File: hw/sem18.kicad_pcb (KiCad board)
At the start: 2 copper layers, 40 x 40 mm, 64 parts, among them J1 USB_C_Receptacle_USB2.0_16P, J4 Prog/debug, J5 Conn_02x04_Odd_Even, Q1 AO3401A, Q2 8205A, Q3 AO3401A, Q4 2N7002, Q5 2N7002, SW1 SW_Push_Shielded, SW2 SW_Push_Shielded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

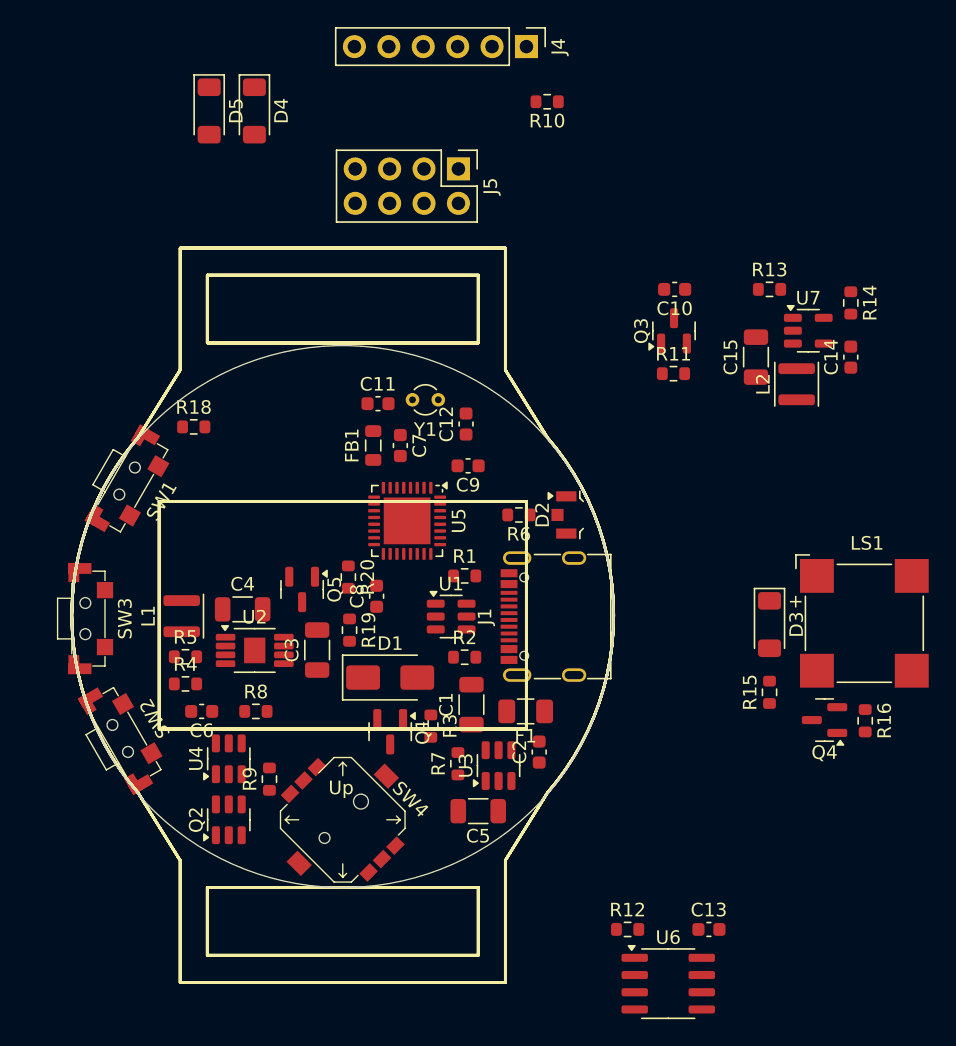
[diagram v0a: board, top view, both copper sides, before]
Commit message: Different microcontroller. Placed most of the components too.
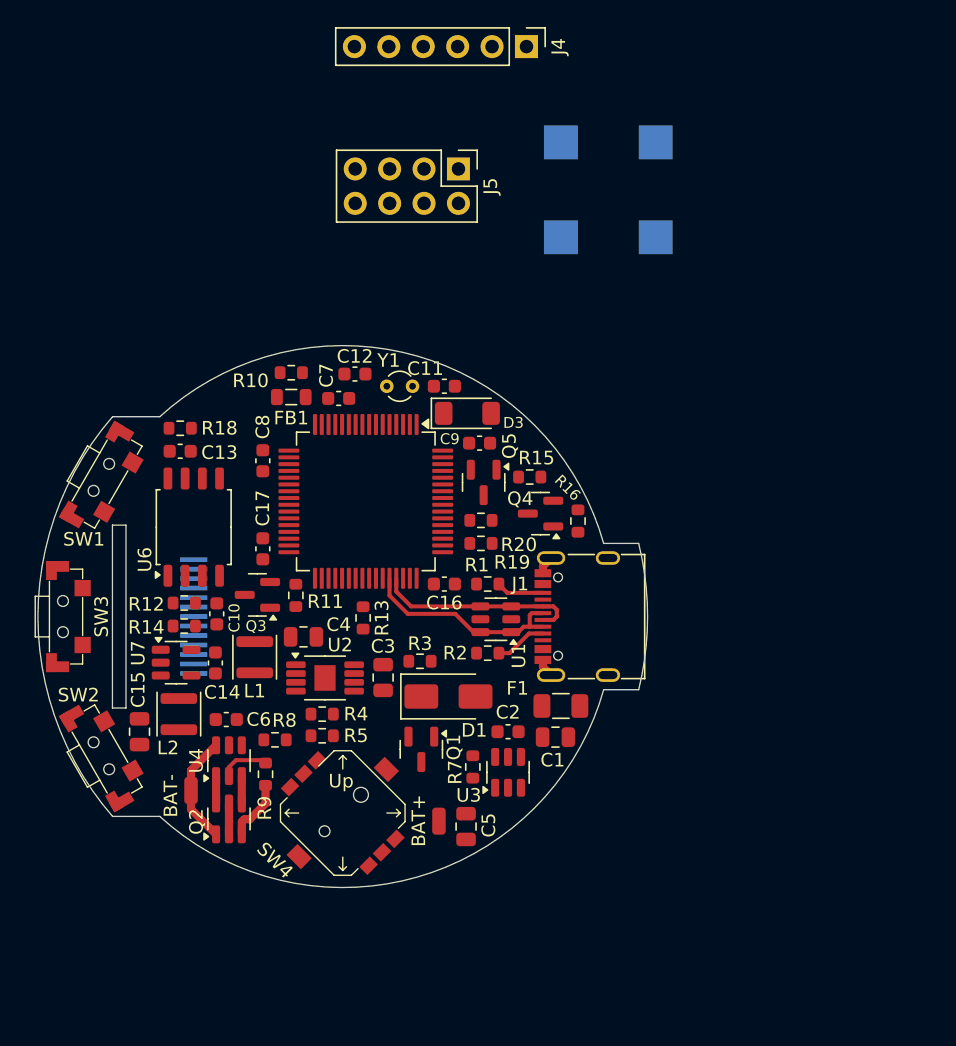
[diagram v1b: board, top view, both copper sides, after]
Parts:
- removed D2: Status, LED_SMD:LED_LiteOn_LTST-S326
- removed D4, D5: LL4148, Diode_SMD:D_MiniMELF
- removed R6: 1k, Resistor_SMD:R_0603_1608Metric
- added C16: 100nF, Capacitor_SMD:C_0603_1608Metric, F.Cu at (167.5, 97.6)
- added C17: 100nF, Capacitor_SMD:C_0603_1608Metric, F.Cu at (154.1, 95.0)
- added J3: Wisevision N114-2413THBIG01-H13, sem18:LCD_ST7789V_13pin, B.Cu at (150.0, 100.0)
- added TP1: Batt+, Connector_Wire:SolderWirePad_1x01_SMD_1x2mm, F.Cu at (167.1, 115.1)
- added TP2: Batt-, Connector_Wire:SolderWirePad_1x01_SMD_1x2mm, F.Cu at (148.8, 112.8)
- C1, C15, C3, C4, C5: footprint Capacitor_SMD:C_1206_3216Metric -> Capacitor_SMD:C_0805_2012Metric
- LS1: moved to B.Cu
- U5: value STM32L432KBUx -> STM32L496RETx; footprint Package_DFN_QFN:QFN-32-1EP_5x5mm_P0.5mm_EP3.45x3.45mm -> Package_QFP:LQFP-64_10x10mm_P0.5mm
- U6: footprint Package_SO:SOIC-8_3.9x4.9mm_P1.27mm -> Package_SO:SOIC-8_5.3x5.3mm_P1.27mm
- moved R14 54.7 mm to (148.3, 100.7), turned to 0 degrees
- moved C15 53.2 mm to (145.0, 108.5), turned to -90 degrees
- moved U7 52.7 mm to (147.7, 103.4)
- moved C13 52.6 mm to (148.0, 87.8), turned to 180 degrees
- moved C14 52.1 mm to (150.6, 103.4), turned to -90 degrees
- moved L2 51.7 mm to (147.9, 107.2)
- moved U6 48.6 mm to (149.0, 93.4), turned to 90 degrees
- moved C10 41.4 mm to (150.7, 99.8), turned to 90 degrees
- moved R12 40.6 mm to (148.3, 99.0)
- moved R13 38.6 mm to (161.5, 100.1), turned to 90 degrees
- moved LS1 37.2 mm to (179.6, 68.5)
- moved Q3 36.4 mm to (153.7, 98.4), turned to 180 degrees
- moved R11 32.3 mm to (156.5, 98.4), turned to 90 degrees
- moved R10 27.5 mm to (156.2, 82.0)
- moved D3 27.2 mm to (169.2, 85.0), turned to 0 degrees
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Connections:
- net /MCU/BUTTONS_CHPLX3 renamed /MCU/BUTTON_SW3
- R19 pad 1: /MCU/BUTTONS_CHPLX2 -> Net-(U5-PA0)
- R20 pad 2: /MCU/BUTTONS_CHPLX2 -> Net-(U5-PA0)
- R5 pad 2: Net-(U2-Mode) -> /MCU/Buck_Mode
- SW2 pad 1: Net-(D4-A) -> GND
- SW2 pad 2: /MCU/BUTTONS_CHPLX2 -> /MCU/BUTTON_SW2
- SW3 pad 1: Net-(D5-A) -> GND
- SW4 pad 1: unconnected-(SW4-Up-Pad1) -> /MCU/BUTTON_SW4_Up
- SW4 pad 2: unconnected-(SW4-Common-Pad2) -> GND
- SW4 pad 3: unconnected-(SW4-Left-Pad3) -> /MCU/BUTTON_SW4_Left
- SW4 pad 4: unconnected-(SW4-Right-Pad4) -> /MCU/BUTTON_SW4_Right
- SW4 pad 5: unconnected-(SW4-Push-Pad5) -> /MCU/BUTTON_SW4_Push
- SW4 pad 6: unconnected-(SW4-Down-Pad6) -> /MCU/BUTTON_SW4_Down
- SW4 pad MP: (no net) -> GND
- U2 pad 3: Net-(U2-Mode) -> /MCU/Buck_Mode
- U3 pad 1: Net-(D2-K1) -> /MCU/Charger_nCharge
- U3 pad 5: Net-(D2-K2) -> /MCU/Charger_Standby
- U5 pad 11: /MCU/BUZZER -> /MCU/BUTTON_SW2
- U5 pad 12: /MCU/FLASH_D3 -> GND
- U5 pad 13: /MCU/FLASH_D2 -> Net-(U5-VDDA)
- U5 pad 14: /MCU/FLASH_D1 -> Net-(U5-PA0)
- U5 pad 15: /MCU/FLASH_D0 -> unconnected-(U5-PA1-Pad15)
- U5 pad 16: GND -> unconnected-(U5-PA2-Pad16)
- U5 pad 17: VDD -> unconnected-(U5-PA3-Pad17)
- U5 pad 18: /MCU/EXT_PA8 -> GND
- U5 pad 19: /MCU/EXT_PA9 -> VDD
- U5 pad 2: Net-(U5-PC14) -> unconnected-(U5-PC13-Pad2)
- U5 pad 20: /MCU/EXT_PA10 -> unconnected-(U5-PA4-Pad20)
- U5 pad 21: /MCU/USB_DM -> /MCU/BUZZER
- U5 pad 22: /MCU/USB_DP -> /MCU/FLASH_D3
- U5 pad 23: /MCU/SWDIO -> /MCU/FLASH_D2
- U5 pad 24: /MCU/SWCLK -> unconnected-(U5-PC4-Pad24)
- U5 pad 25: /MCU/LCD_nSS -> unconnected-(U5-PC5-Pad25)
- U5 pad 26: /MCU/LCD_nPWR -> /MCU/FLASH_D1
- U5 pad 27: /MCU/LCD_DC -> /MCU/FLASH_D0
- U5 pad 28: /MCU/LCD_SDAT -> /MCU/Buck_Mode
- U5 pad 29: /MCU/LCD_BL -> /MCU/FLASH_SCK
- U5 pad 3: Net-(U5-PC15) -> Net-(U5-PC14)
- U5 pad 30: /MCU/BUTTONS_CHPLX1 -> /MCU/FLASH_nCS
- U5 pad 31: /MCU/BUTTON_WAKE -> GND
- U5 pad 32: GND -> VDD
- U5 pad 33: GND -> /MCU/LCD_nSS
- U5 pad 4: /MCU/nRST -> Net-(U5-PC15)
- U5 pad 5: Net-(U5-VDDA) -> unconnected-(U5-PH0-Pad5)
- U5 pad 6: /MCU/BUTTONS_CHPLX2 -> unconnected-(U5-PH1-Pad6)
- U5 pad 7: /MCU/LCD_SCK -> /MCU/nRST
- U5 pad 8: /MCU/FLASH_nCS -> unconnected-(U5-PC0-Pad8)
- U5 pad 9: /MCU/FLASH_SCK -> unconnected-(U5-PC1-Pad9)
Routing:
- net /MCU/USB_DM: track 0.00 -> 15.8 mm
- net /MCU/USB_DP: track 0.00 -> 15.0 mm
- net Net-(Q2-D1): track 0.00 -> 8.11 mm
- net GND: track 0.00 -> 7.31 mm
- net Net-(J1-CC1): track 0.00 -> 3.85 mm
- net Net-(U4-CS): track 0.00 -> 3.66 mm
- net Net-(J1-CC2): track 0.00 -> 3.53 mm
- net Net-(Q2-S1/D2-Pad2): track 0.00 -> 2.28 mm
- net Net-(Q2-G2): track 0.00 -> 2.02 mm
- net Net-(Q2-G1): track 0.00 -> 2.02 mm
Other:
- board size 40 x 40 mm -> 45 x 40 mm
- board text added: "BAT+"
- board text added: "BAT-"

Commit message: Placed remaining components.
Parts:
- removed J5: Conn_02x04_Odd_Even, Connector_PinHeader_2.54mm:PinHeader_2x04_P2.54mm_Vertical
- added J2: FPC 8 pin, Connector_FFC-FPC:Hirose_FH12-8S-0.5SH_1x08-1MP_P0.50mm_Horizontal, B.Cu at (160.0, 97.0)
- added SW8: Reset, Button_Switch_SMD:SW_SPST_TL3342, B.Cu at (158.6, 85.5)
- added TP3: RTC calibration, TestPoint:TestPoint_Pad_D1.0mm, B.Cu at (163.3, 88.1)
- J4: footprint Connector_PinHeader_2.54mm:PinHeader_1x06_P2.54mm_Vertical -> sem18:ProgConnector_5pin; moved to B.Cu
- LS1: footprint Buzzer_Beeper:MagneticBuzzer_CUI_CMT-8504-100-SMT -> sem18:Buzzer_8.5x8.5mm
- moved J4 34.8 mm to (152.5, 85.6), turned to 60 degrees
- moved LS1 25.6 mm to (173.8, 93.5), turned to 45 degrees
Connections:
- J4 pad 1: VDD -> /MCU/SWCLK
- J4 pad 2: /MCU/SWCLK -> /MCU/SWDIO
- J4 pad 4: /MCU/SWDIO -> VDD
- U5 pad 2: unconnected-(U5-PC13-Pad2) -> Net-(U5-PC13)

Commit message: Replaced extension connector.
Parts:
- J2: value FPC 8 pin -> FPC; footprint Connector_FFC-FPC:Hirose_FH12-8S-0.5SH_1x08-1MP_P0.50mm_Horizontal -> Connector_FFC-FPC:Hirose_FH12-10S-0.5SH_1x10-1MP_P0.50mm_Horizontal
- TP1, TP2: moved to B.Cu
- moved J2 2.17 mm to (162.1, 96.4)
- turned R18 to 180 degrees
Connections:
- R18 pad 1: /MCU/BUTTON_WAKE -> GND
- R18 pad 2: VDD -> /MCU/BUTTON_WAKE
- SW1 pad 1: GND -> /MCU/BUTTON_WAKE
- SW1 pad 2: /MCU/BUTTON_WAKE -> VDD
- U5 pad 8: unconnected-(U5-PC0-Pad8) -> /MCU/EXT_PC0
- U5 pad 9: unconnected-(U5-PC1-Pad9) -> /MCU/EXT_PC1

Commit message: Routing in progress.
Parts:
- removed Q5: 2N7002, Package_TO_SOT_SMD:SOT-23
- moved R5 3.47 mm to (155.4, 107.2), turned to 0 degrees
- moved J2 0.60 mm to (161.5, 96.4)
- moved C17 0.40 mm to (153.7, 95.0)
- moved C13 0.10 mm to (147.9, 87.8)
- moved R18 0.10 mm to (147.9, 86.1)
- turned R10 to 0 degrees
- turned R14 to 180 degrees
- turned SW8 to -90 degrees
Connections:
- J2 pad 1: /MCU/EXT_PA8 -> /MCU/EXT_PA10
- J2 pad 4: /MCU/LCD_SDAT -> /MCU/EXT_PA8
- J2 pad 5: /MCU/EXT_PA10 -> /MCU/LCD_SDAT
- R20 pad 1: Net-(Q5-D) -> /MCU/VMEAS_GND
- SW1 pad 1: /MCU/BUTTON_WAKE -> VDD
- SW1 pad 2: VDD -> /MCU/BUTTON_WAKE
- U5 pad 10: /MCU/BUTTON_SW3 -> unconnected-(U5-PC2-Pad10)
- U5 pad 11: /MCU/BUTTON_SW2 -> unconnected-(U5-PC3-Pad11)
- U5 pad 21: /MCU/BUZZER -> unconnected-(U5-PA5-Pad21)
- U5 pad 24: unconnected-(U5-PC4-Pad24) -> /MCU/BUTTON_SW2
- U5 pad 25: unconnected-(U5-PC5-Pad25) -> /MCU/BUTTON_SW3
- U5 pad 50: /MCU/BUTTON_SW4_Up -> /MCU/BUTTON_SW4_Right
- U5 pad 51: /MCU/BUTTON_SW4_Down -> /MCU/BUTTON_SW4_Left
- U5 pad 52: /MCU/BUTTON_SW4_Left -> /MCU/BUTTON_SW4_Push
- U5 pad 53: /MCU/BUTTON_SW4_Right -> /MCU/BUTTON_SW4_Up
- U5 pad 55: /MCU/BUTTON_SW4_Push -> /MCU/BUTTON_SW4_Down
- U5 pad 58: unconnected-(U5-PB6-Pad58) -> /MCU/VMEAS_GND
- U5 pad 59: unconnected-(U5-PB7-Pad59) -> /MCU/BUZZER
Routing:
- net VDD: track 0.00 -> 102.6 mm, vias 0 -> 5
- net GND: track 7.31 -> 98.3 mm, vias 0 -> 129
- net +VSW: track 0.00 -> 56.1 mm, vias 0 -> 7
- net /MCU/BUTTON_SW2: track 0.00 -> 39.2 mm, vias 0 -> 2
- net /MCU/BUTTON_WAKE: track 0.00 -> 34.4 mm, vias 0 -> 2
- net /MCU/BUTTON_SW4_Down: track 0.00 -> 30.6 mm, vias 0 -> 2
- net /MCU/BUTTON_SW3: track 0.00 -> 27.9 mm, vias 0 -> 2
- net /MCU/BUTTON_SW4_Push: track 0.00 -> 27.3 mm, vias 0 -> 2
- net /MCU/BUTTON_SW4_Left: track 0.00 -> 25.7 mm, vias 0 -> 2
- net /MCU/BUTTON_SW4_Right: track 0.00 -> 25.1 mm, vias 0 -> 2
- net /MCU/Charger_nCharge: track 0.00 -> 24.5 mm, vias 0 -> 4
- net /MCU/BUTTON_SW4_Up: track 0.00 -> 24.4 mm, vias 0 -> 2
- net /MCU/Charger_Standby: track 0.00 -> 24.3 mm, vias 0 -> 4
- net /Power/VBAT: track 0.00 -> 23.6 mm, vias 0 -> 3
- net /MCU/nRST: track 0.00 -> 22.6 mm, vias 0 -> 3
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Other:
- board text added: "Vesztettem"

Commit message: Routed.
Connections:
- U5 pad 37: /MCU/LCD_BL -> /MCU/LCD_nPWR
- U5 pad 38: /MCU/LCD_nPWR -> /MCU/LCD_BL
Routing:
- net /MCU/LCD_BL: track 0.00 -> 23.3 mm, vias 0 -> 2
- net /MCU/LCD_SDAT: track 2.41 -> 24.8 mm, vias 0 -> 1
- net GND: track 98.3 -> 115.3 mm, vias 129 -> 173
- net /MCU/LCD_SCK: track 4.44 -> 20.7 mm
- net Net-(J3-Pin_12): track 3.23 -> 17.4 mm, vias 0 -> 1
- net /MCU/LCD_DC: track 0.00 -> 14.2 mm, vias 0 -> 1
- net +VSW: track 56.1 -> 69.7 mm, vias 7 -> 9
- net /MCU/LCD_nPWR: track 1.94 -> 13.6 mm, vias 0 -> 2
- net /MCU/LCD_nSS: track 1.28 -> 12.9 mm, vias 0 -> 1
- net Net-(J3-Pin_11): track 2.60 -> 10.6 mm, vias 0 -> 1
- net Net-(J3-Pin_10): track 2.32 -> 9.90 mm, vias 0 -> 2
- net /MCU/Buck_Mode: track 19.0 -> 23.8 mm
- net /Power/USBPOWER_IN: track 17.8 -> 22.3 mm
- net /MCU/FLASH_D1: track 8.73 -> 11.2 mm
- net /MCU/BUTTON_WAKE: track 34.4 -> 33.5 mm
- added copper zone on B.Cu, net GND
- added copper zone on F.Cu, net GND

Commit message: Supposedly finished.
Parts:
- added G***: LOGO, sem18:semlogo, B.Cu at (160.0, 108.1)
- added TP4: Ground, TestPoint:TestPoint_Pad_D1.0mm, B.Cu at (163.8, 85.5)
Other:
- board text added: "Reset"
- board text added: "Rev.A"
- board text added: "SEM18 {dblquote}karóra{dblquote} by Kristóf"

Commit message: Sent to fab.
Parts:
- added T1: Tab, PCM_kikit:Tab, F.Cu at (160.0, 70.0)
- added T2: Tab, PCM_kikit:Tab, F.Cu at (160.0, 130.0)
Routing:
- net GND: vias 173 -> 174
- added copper zone on In1.Cu, net GND
- added copper zone on In2.Cu, net GND
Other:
- copper layers 2 -> 4

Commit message: Changed naming of the upper left button.
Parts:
- C11, C12: value TBD -> 20pF
- R15: value 1k -> 100
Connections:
- net /MCU/BUTTON_WAKE renamed /MCU/BUTTON_SW1
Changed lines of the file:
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@@
 	(net 39 "/MCU/FLASH_nCS")
 	(net 40 "Net-(J3-Pin_11)")
-	(net 41 "/MCU/BUTTON_WAKE")
+	(net 41 "/MCU/BUTTON_SW1")
 	(net 42 "/MCU/USB_DP")
 	(net 43 "/MCU/USB_DM")
@@
 			)
 		)
-		(property "Value" "TBD"
+		(property "Value" "20pF"
 			(at 0 1.43 0)
 			(layer "F.Fab")
@@
 			(layers "F.Cu" "F.Mask" "F.Paste")
 			(roundrect_rratio 0.25)
-			(net 41 "/MCU/BUTTON_WAKE")
+			(net 41 "/MCU/BUTTON_SW1")
 			(pinfunction "PH3")
 			(pintype "bidirectional")
@@
 			)
 		)
-		(property "Value" "1k"
+		(property "Value" "100"
 			(at 0 1.43 0)
 			(layer "F.Fab")
@@
 			(size 1.2 1.2)
 			(layers "F.Cu" "F.Mask" "F.Paste")
-			(net 41 "/MCU/BUTTON_WAKE")
+			(net 41 "/MCU/BUTTON_SW1")
 			(pinfunction "2")
 			(pintype "passive")
@@
 			(layers "F.Cu" "F.Mask" "F.Paste")
 			(roundrect_rratio 0.25)
-			(net 41 "/MCU/BUTTON_WAKE")
+			(net 41 "/MCU/BUTTON_SW1")
 			(pintype "passive")
 		)
@@
 			)
 		)
-		(property "Value" "TBD"
+		(property "Value" "20pF"
 			(at 0 1.43 0)
 			(layer "F.Fab")
@@
 		(embedded_fonts no)
 	)
-	(gr_arc
-		(start 144.887414 113.099988)
-		(mid 140 100)
-		(end 144.887418 86.900007)
+	(gr_line
+		(start 148 118.1)
+		(end 144.887418 113.099993)
 		(stroke
 			(width 0.2)
@@
 		(layer "Dwgs.User")
 	)
-	(gr_arc
-		(start 144.887418 113.099993)
-		(mid 140 100)
-		(end 144.887414 86.900012)
+	(gr_line
+		(start 148 81.9)
+		(end 144.887418 86.900007)
 		(stroke
 			(width 0.2)
@@
 	)
 	(gr_line
-		(start 146.45 91.6)
-		(end 146.45 108.4)
+		(start 172 81.9)
+		(end 175.112582 86.900006)
 		(stroke
 			(width 0.2)
@@
 	)
 	(gr_line
-		(start 146.45 108.4)
-		(end 173.55 108.4)
+		(start 172 118.1)
+		(end 175.112586 113.099987)
 		(stroke
 			(width 0.2)
@@
 	)
 	(gr_line
-		(start 148 72.9)
-		(end 148 81.9)
+		(start 148 127.1)
+		(end 172 127.1)
 		(stroke
 			(width 0.2)
@@
 	)
 	(gr_line
-		(start 148 81.9)
-		(end 144.887414 86.900012)
+		(start 146.45 91.6)
+		(end 146.45 108.4)
 		(stroke
 			(width 0.2)
@@
 	)
 	(gr_line
-		(start 148 81.9)
-		(end 144.887418 86.900007)
+		(start 170 74.9)
+		(end 150 74.9)
 		(stroke
 			(width 0.2)
@@
 	)
 	(gr_line
-		(start 148 118.1)
-		(end 144.887414 113.099988)
+		(start 148 72.9)
+		(end 148 81.9)
 		(stroke
 			(width 0.2)
@@
 	(gr_line
 		(start 148 118.1)
-		(end 144.887418 113.099993)
+		(end 144.887414 113.099988)
 		(stroke
 			(width 0.2)
@@
 	)
 	(gr_line
-		(start 148 118.1)
-		(end 148 127.1)
+		(start 150 125.1)
+		(end 170 125.1)
 		(stroke
 			(width 0.2)
@@
 	)
 	(gr_line
-		(start 148 127.1)
-		(end 172 127.1)
+		(start 170 125.1)
+		(end 170 120.1)
 		(stroke
 			(width 0.2)
@@
 	)
 	(gr_line
-		(start 150 79.9)
-		(end 170 79.9)
+		(start 172 118.1)
+		(end 175.112582 113.099994)
 		(stroke
 			(width 0.2)
@@
 	)
 	(gr_line
-		(start 150 120.1)
-		(end 150 125.1)
+		(start 172 127.1)
+		(end 172 118.1)
 		(stroke
 			(width 0.2)
@@
 	)
 	(gr_line
-		(start 150 125.1)
-		(end 170 125.1)
+		(start 146.45 108.4)
+		(end 173.55 108.4)
 		(stroke
 			(width 0.2)
@@
 	)
 	(gr_line
-		(start 170 74.9)
-		(end 150 74.9)
+		(start 173.55 108.4)
+		(end 173.55 91.6)
 		(stroke
 			(width 0.2)
@@
 	)
 	(gr_line
-		(start 170 79.9)
-		(end 170 74.9)
+		(start 173.55 91.6)
+		(end 146.45 91.6)
 		(stroke
 			(width 0.2)
@@
 		(layer "Dwgs.User")
 	)
-	(gr_line
-		(start 170 125.1)
-		(end 170 120.1)
+	(gr_arc
+		(start 175.112582 86.900006)
+		(mid 180 100)
+		(end 175.112586 113.099987)
 		(stroke
 			(width 0.2)
@@
 		(layer "Dwgs.User")
 	)
-	(gr_line
-		(start 172 72.9)
-		(end 148 72.9)
+	(gr_arc
+		(start 144.887418 113.099993)
+		(mid 140 100)
+		(end 144.887414 86.900012)
 		(stroke
 			(width 0.2)
@@
 	)
 	(gr_line
-		(start 172 81.9)
-		(end 172 72.9)
+		(start 170 79.9)
+		(end 170 74.9)
 		(stroke
 			(width 0.2)
@@
 	)
 	(gr_line
-		(start 172 81.9)
-		(end 175.112582 86.900006)
+		(start 150 120.1)
+		(end 150 125.1)
 		(stroke
 			(width 0.2)
@@
 	)
 	(gr_line
-		(start 172 118.1)
-		(end 175.112582 113.099994)
+		(start 172 72.9)
+		(end 148 72.9)
 		(stroke
 			(width 0.2)
@@
 	)
 	(gr_line
-		(start 172 118.1)
-		(end 175.112586 113.099987)
+		(start 150 79.9)
+		(end 170 79.9)
 		(stroke
 			(width 0.2)
@@
 	)
 	(gr_line
-		(start 172 127.1)
-		(end 172 118.1)
+		(start 172 81.9)
+		(end 172 72.9)
 		(stroke
 			(width 0.2)
@@
 	)
 	(gr_line
-		(start 173.55 91.6)
-		(end 146.45 91.6)
+		(start 148 81.9)
+		(end 144.887414 86.900012)
 		(stroke
 			(width 0.2)
@@
 		(layer "Dwgs.User")
 	)
-	(gr_line
-		(start 173.55 108.4)
-		(end 173.55 91.6)
+	(gr_arc
+		(start 175.112582 86.900007)
+		(mid 180 100)
+		(end 175.112582 113.099994)
 		(stroke
 			(width 0.2)
@@
 		(layer "Dwgs.User")
 	)
-	(gr_arc
-		(start 175.112582 86.900007)
-		(mid 180 100)
-		(end 175.112582 113.099994)
+	(gr_line
+		(start 148 118.1)
+		(end 148 127.1)
 		(stroke
 			(width 0.2)
@@
 	)
 	(gr_arc
-		(start 175.112582 86.900006)
-		(mid 180 100)
-		(end 175.112586 113.099987)
+		(start 144.887414 113.099988)
+		(mid 140 100)
+		(end 144.887418 86.900007)
 		(stroke
 			(width 0.2)
@@
 		(layer "Dwgs.User")
 	)
+	(gr_arc
+		(start 146.493058 85.25)
+		(mid 165.488352 80.767788)
+		(end 179.257206 94.6)
+		(stroke
+			(width 0.05)
+			(type default)
+		)
+		(layer "Edge.Cuts")
+	)
 	(gr_rect
 		(start 143 93.25)
@@
 		(layer "Edge.Cuts")
 	)
-	(gr_arc
-		(start 143.009194 114.75)
-		(mid 137.5 100)
-		(end 143.009194 85.25)
+	(gr_line
+		(start 179.257206 94.6)
+		(end 181.842389 94.6)
 		(stroke
 			(width 0.05)
@@
 	)
 	(gr_line
-		(start 146.493059 85.25)
-		(end 143.009194 85.25)
+		(start 146.493059 114.75)
+		(end 143.009194 114.75)
 		(stroke
 			(width 0.05)
@@
 		(layer "Edge.Cuts")
 	)
-	(gr_arc
-		(start 146.493058 85.25)
-		(mid 165.488352 80.767788)
-		(end 179.257206 94.6)
+	(gr_line
+		(start 179.257206 105.4)
+		(end 181.842389 105.4)
 		(stroke
 			(width 0.05)
@@
 		(layer "Edge.Cuts")
 	)
-	(gr_line
-		(start 146.493059 114.75)
-		(end 143.009194 114.75)
+	(gr_arc
+		(start 143.009194 114.75)
+		(mid 137.5 100)
+		(end 143.009194 85.25)
 		(stroke
 			(width 0.05)
@@
 	)
 	(gr_line
-		(start 179.257206 94.6)
-		(end 181.842389 94.6)
+		(start 146.493059 85.25)
+		(end 143.009194 85.25)
 		(stroke
 			(width 0.05)
@@
 		(layer "Edge.Cuts")
 	)
-	(gr_line
-		(start 179.257206 105.4)
-		(end 181.842389 105.4)
-		(stroke
-			(width 0.05)
-			(type default)
-		)
-		(layer "Edge.Cuts")
-	)
 	(gr_arc
 		(start 181.842389 94.6)
@@
 		)
 	)
-	(gr_text "Reset"
-		(at 155.6 86.3 90)
+	(gr_text "SEM18 {dblquote}karóra{dblquote}\nby Kristóf"
+		(at 181.6 97.9 0)
 		(layer "B.SilkS")
 		(effects
 			(font
-				(size 0.8 0.8)
-				(thickness 0.15)
+				(size 1 1)
+				(thickness 0.2)
 				(bold yes)
 			)
-			(justify left bottom mirror)
+			(justify left top mirror)
 		)
 	)
@@
 		)
 	)
-	(gr_text "BAT+"
-		(at 166.3 113.4 90)
+	(gr_text "Reset"
+		(at 155.6 86.3 90)
 		(layer "B.SilkS")
 		(effects
 			(font
-				(size 1 1)
-				(thickness 0.1)
+				(size 0.8 0.8)
+				(thickness 0.15)
+				(bold yes)
 			)
 			(justify left bottom mirror)
 		)
 	)
-	(gr_text "SEM18 {dblquote}karóra{dblquote}\nby Kristóf"
-		(at 181.6 97.9 0)
+	(gr_text "BAT+"
+		(at 166.3 113.4 90)
 		(layer "B.SilkS")
 		(effects
 			(font
 				(size 1 1)
-				(thickness 0.2)
-				(bold yes)
+				(thickness 0.1)
 			)
-			(justify left top mirror)
+			(justify left bottom mirror)
 		)
 	)
